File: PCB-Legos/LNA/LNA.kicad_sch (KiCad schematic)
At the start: 36 parts, among them J1 Conn_Coaxial, J2 Conn_Coaxial, J3 Conn_Coaxial, U1 LP2985XX-N, U2 LNA-TP3M9037, U3 QPQ1907, U4 LP2985XX-N, U5 LNA-TP3M9037, U6 QPQ1907

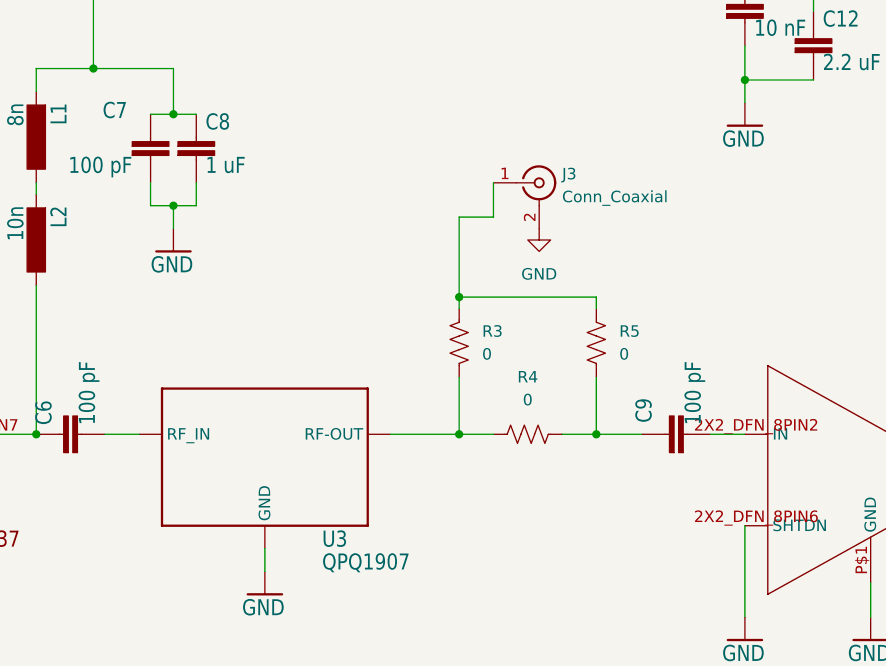
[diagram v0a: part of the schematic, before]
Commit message: LNA Test Board
LNA Test Board. Has ability to test each stage separately.
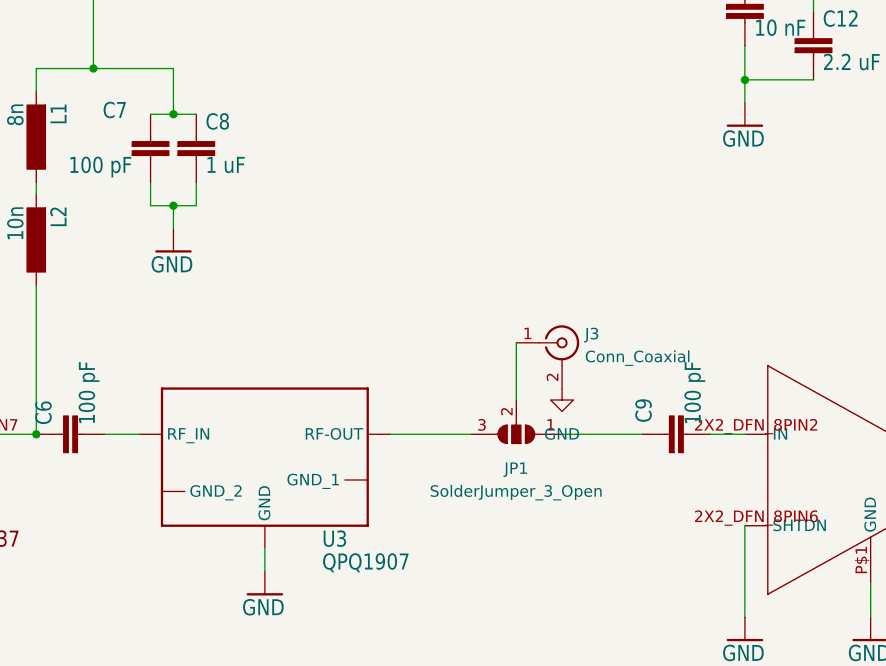
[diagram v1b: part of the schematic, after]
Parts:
- removed R3, R4, R5: 0, HGS_Reflector:.0603-B-NOSILK, symbol Device:R_US
- added JP1: SolderJumper_3_Open, Jumper:SolderJumper-3_P1.3mm_Open_Pad1.0x1.5mm_NumberLabels, symbol Jumper:SolderJumper_3_Open
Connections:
- net at U3.OUTPUT (RF-OUT): now also JP1.3 (B)
- net at C9.1: now also JP1.1 (A)
- net at J3.1 (In): now also JP1.2 (C)
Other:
- moved on the sheet: J3
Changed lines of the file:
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@@
   (junction (at 160.02 54.61) (diameter 0) (color 0 0 0 0)
   )
-  (junction (at 135.89 127) (diameter 0) (color 0 0 0 0)
-  )
   (junction (at 212.09 91.44) (diameter 0) (color 0 0 0 0)
   )
@@
   (junction (at 203.2 86.36) (diameter 0) (color 0 0 0 0)
   )
-  (junction (at 151.13 127) (diameter 0) (color 0 0 0 0)
-  )
-  (junction (at 135.89 111.76) (diameter 0) (color 0 0 0 0)
-  )
   (junction (at 167.64 87.63) (diameter 0) (color 0 0 0 0)
   )
@@
     (stroke (width 0) (type default) (color 0 0 0 0))
   )
-  (wire (pts (xy 128.27 127) (xy 135.89 127))
-    (stroke (width 0) (type default) (color 0 0 0 0))
-  )
-  (wire (pts (xy 135.89 111.76) (xy 151.13 111.76))
+  (wire (pts (xy 128.27 127) (xy 137.16 127))
     (stroke (width 0) (type default) (color 0 0 0 0))
   )
@@
     (stroke (width 0) (type default) (color 0 0 0 0))
   )
-  (wire (pts (xy 139.7 99.06) (xy 139.7 102.87))
-    (stroke (width 0) (type default) (color 0 0 0 0))
-  )
   (wire (pts (xy 224.79 144.78) (xy 224.79 147.32))
     (stroke (width 0) (type default) (color 0 0 0 0))
@@
     (stroke (width 0) (type default) (color 0 0 0 0))
   )
-  (wire (pts (xy 151.13 127) (xy 156.21 127))
-    (stroke (width 0) (type default) (color 0 0 0 0))
-  )
   (wire (pts (xy 67.31 140.97) (xy 67.31 138.43))
     (stroke (width 0) (type default) (color 0 0 0 0))
@@
     (stroke (width 0) (type default) (color 0 0 0 0))
   )
-  (wire (pts (xy 135.89 111.76) (xy 135.89 113.03))
-    (stroke (width 0) (type default) (color 0 0 0 0))
-  )
   (wire (pts (xy 199.39 132.08) (xy 196.85 132.08))
     (stroke (width 0) (type default) (color 0 0 0 0))
@@
     (stroke (width 0) (type default) (color 0 0 0 0))
   )
-  (wire (pts (xy 135.89 120.65) (xy 135.89 127))
-    (stroke (width 0) (type default) (color 0 0 0 0))
-  )
-  (wire (pts (xy 151.13 111.76) (xy 151.13 113.03))
-    (stroke (width 0) (type default) (color 0 0 0 0))
-  )
   (wire (pts (xy 59.69 90.17) (xy 59.69 87.63))
     (stroke (width 0) (type default) (color 0 0 0 0))
@@
     (stroke (width 0) (type default) (color 0 0 0 0))
   )
-  (wire (pts (xy 151.13 120.65) (xy 151.13 127))
-    (stroke (width 0) (type default) (color 0 0 0 0))
-  )
   (wire (pts (xy 67.31 44.45) (xy 67.31 40.64))
     (stroke (width 0) (type default) (color 0 0 0 0))
@@
     (stroke (width 0) (type default) (color 0 0 0 0))
   )
-  (wire (pts (xy 139.7 102.87) (xy 135.89 102.87))
-    (stroke (width 0) (type default) (color 0 0 0 0))
-  )
-  (wire (pts (xy 147.32 127) (xy 151.13 127))
+  (wire (pts (xy 147.32 127) (xy 156.21 127))
     (stroke (width 0) (type default) (color 0 0 0 0))
   )
@@
     (stroke (width 0) (type default) (color 0 0 0 0))
   )
+  (wire (pts (xy 142.24 116.84) (xy 142.24 123.19))
+    (stroke (width 0) (type default) (color 0 0 0 0))
+  )
   (wire (pts (xy 167.64 44.45) (xy 167.64 40.64))
     (stroke (width 0) (type default) (color 0 0 0 0))
@@
   )
   (wire (pts (xy 88.9 86.36) (xy 95.25 86.36))
-    (stroke (width 0) (type default) (color 0 0 0 0))
-  )
-  (wire (pts (xy 135.89 102.87) (xy 135.89 111.76))
-    (stroke (width 0) (type default) (color 0 0 0 0))
-  )
-  (wire (pts (xy 135.89 127) (xy 139.7 127))
     (stroke (width 0) (type default) (color 0 0 0 0))
   )
@@
     (pin "OUTPUT")
   )
-  (symbol (lib_id "power:GND") (at 144.78 104.14 0) (unit 1)
+  (symbol (lib_id "power:GND") (at 147.32 121.92 0) (unit 1)
     (in_bom yes) (on_board yes) (fields_autoplaced)
-    (property "Reference" "#PWR0102" (id 0) (at 144.78 110.49 0)
-      (effects (font (size 1.27 1.27)) hide)
-    )
-    (property "Value" "GND" (id 1) (at 144.78 109.22 0))
-    (property "Footprint" "" (id 2) (at 144.78 104.14 0)
-      (effects (font (size 1.27 1.27)) hide)
-    )
-    (property "Datasheet" "" (id 3) (at 144.78 104.14 0)
+    (property "Reference" "#PWR0102" (id 0) (at 147.32 128.27 0)
+      (effects (font (size 1.27 1.27)) hide)
+    )
+    (property "Value" "GND" (id 1) (at 147.32 127 0))
+    (property "Footprint" "" (id 2) (at 147.32 121.92 0)
+      (effects (font (size 1.27 1.27)) hide)
+    )
+    (property "Datasheet" "" (id 3) (at 147.32 121.92 0)
       (effects (font (size 1.27 1.27)) hide)
     )
@@
     (pin "2")
   )
-  (symbol (lib_id "Device:R_US") (at 143.51 127 90) (unit 1)
-    (in_bom yes) (on_board yes) (fields_autoplaced)
-    (property "Reference" "R4" (id 0) (at 143.51 120.65 90))
-    (property "Value" "0" (id 1) (at 143.51 123.19 90))
-    (property "Footprint" "HGS_Reflector:.0603-B-NOSILK" (id 2) (at 143.764 125.984 90)
-      (effects (font (size 1.27 1.27)) hide)
-    )
-    (property "Datasheet" "~" (id 3) (at 143.51 127 0)
-      (effects (font (size 1.27 1.27)) hide)
-    )
-    (pin "1")
-    (pin "2")
-  )
   (symbol (lib_id "HGS_Reflector-eagle-import:GND") (at 224.79 149.86 0) (unit 1)
     (in_bom yes) (on_board yes)
@@
     (pin "2")
   )
-  (symbol (lib_id "Connector:Conn_Coaxial") (at 144.78 99.06 0) (unit 1)
+  (symbol (lib_id "Connector:Conn_Coaxial") (at 147.32 116.84 0) (unit 1)
     (in_bom yes) (on_board yes) (fields_autoplaced)
-    (property "Reference" "J3" (id 0) (at 147.32 98.0831 0)
+    (property "Reference" "J3" (id 0) (at 149.86 115.8631 0)
       (effects (font (size 1.27 1.27)) (justify left))
     )
-    (property "Value" "Conn_Coaxial" (id 1) (at 147.32 100.6231 0)
+    (property "Value" "Conn_Coaxial" (id 1) (at 149.86 118.4031 0)
       (effects (font (size 1.27 1.27)) (justify left))
     )
-    (property "Footprint" "Connector_Coaxial:SMA_Molex_73251-1153_EdgeMount_Horizontal" (id 2) (at 144.78 99.06 0)
-      (effects (font (size 1.27 1.27)) hide)
-    )
-    (property "Datasheet" " ~" (id 3) (at 144.78 99.06 0)
+    (property "Footprint" "Connector_Coaxial:SMA_Molex_73251-1153_EdgeMount_Horizontal" (id 2) (at 147.32 116.84 0)
+      (effects (font (size 1.27 1.27)) hide)
+    )
+    (property "Datasheet" " ~" (id 3) (at 147.32 116.84 0)
       (effects (font (size 1.27 1.27)) hide)
     )
@@
     )
     (pin "1")
+  )
+  (symbol (lib_id "Jumper:SolderJumper_3_Open") (at 142.24 127 180) (unit 1)
+    (in_bom yes) (on_board yes) (fields_autoplaced)
+    (property "Reference" "JP1" (id 0) (at 142.24 130.81 0))
+    (property "Value" "SolderJumper_3_Open" (id 1) (at 142.24 133.35 0))
+    (property "Footprint" "Jumper:SolderJumper-3_P1.3mm_Open_Pad1.0x1.5mm_NumberLabels" (id 2) (at 142.24 127 0)
+      (effects (font (size 1.27 1.27)) hide)
+    )
+    (property "Datasheet" "~" (id 3) (at 142.24 127 0)
+      (effects (font (size 1.27 1.27)) hide)
+    )
+    (pin "1")
+    (pin "2")
+    (pin "3")
   )
   (symbol (lib_id "HGS_Reflector-eagle-import:GND") (at 181.61 149.86 0) (unit 1)
@@
     (pin "1")
   )
-  (symbol (lib_id "Device:R_US") (at 151.13 116.84 0) (unit 1)
-    (in_bom yes) (on_board yes) (fields_autoplaced)
-    (property "Reference" "R5" (id 0) (at 153.67 115.5699 0)
-      (effects (font (size 1.27 1.27)) (justify left))
-    )
-    (property "Value" "0" (id 1) (at 153.67 118.1099 0)
-      (effects (font (size 1.27 1.27)) (justify left))
-    )
-    (property "Footprint" "HGS_Reflector:.0603-B-NOSILK" (id 2) (at 152.146 117.094 90)
-      (effects (font (size 1.27 1.27)) hide)
-    )
-    (property "Datasheet" "~" (id 3) (at 151.13 116.84 0)
-      (effects (font (size 1.27 1.27)) hide)
-    )
-    (pin "1")
-    (pin "2")
-  )
   (symbol (lib_id "HGS_Reflector-eagle-import:VUSB") (at 243.84 44.45 180) (unit 1)
     (in_bom yes) (on_board yes)
@@
     (pin "1")
   )
-  (symbol (lib_id "Device:R_US") (at 135.89 116.84 0) (mirror y) (unit 1)
-    (in_bom yes) (on_board yes) (fields_autoplaced)
-    (property "Reference" "R3" (id 0) (at 138.43 115.5699 0)
-      (effects (font (size 1.27 1.27)) (justify right))
-    )
-    (property "Value" "0" (id 1) (at 138.43 118.1099 0)
-      (effects (font (size 1.27 1.27)) (justify right))
-    )
-    (property "Footprint" "HGS_Reflector:.0603-B-NOSILK" (id 2) (at 134.874 117.094 90)
-      (effects (font (size 1.27 1.27)) hide)
-    )
-    (property "Datasheet" "~" (id 3) (at 135.89 116.84 0)
-      (effects (font (size 1.27 1.27)) hide)
-    )
-    (pin "1")
-    (pin "2")
-  )
   (symbol (lib_id "HGS_Reflector-eagle-import:C-EU0402-C-NOSILK") (at 201.93 132.08 90) (unit 1)
     (in_bom yes) (on_board yes)
@@
     (pin "1")
   )
-  (symbol (lib_id "HGS_Reflector-eagle-import:QPQ1907") (at 114.3 129.54 0) (unit 1)
+  (symbol (lib_name "QPQ1907_1") (lib_id "HGS_Reflector-eagle-import:QPQ1907") (at 114.3 129.54 0) (unit 1)
     (in_bom yes) (on_board yes)
     (property "Reference" "U3" (id 0) (at 120.65 139.7 0)
@@
     (pin "INPUT")
     (pin "OUTPUT")
+    (pin "")
+    (pin "")
   )
   (sheet_instances
@@
       (reference "J3") (unit 1) (value "Conn_Coaxial") (footprint "Connector_Coaxial:SMA_Molex_73251-1153_EdgeMount_Horizontal")
     )
+    (path "/742f6656-c86d-41c0-937e-ef6ded3bd482"
+      (reference "JP1") (unit 1) (value "SolderJumper_3_Open") (footprint "Jumper:SolderJumper-3_P1.3mm_Open_Pad1.0x1.5mm_NumberLabels")
+    )
     (path "/29f4961c-cbd7-42a0-91e7-8ae77405e061"
       (reference "L1") (unit 1) (value "8n") (footprint "HGS_Reflector:L3216C")
@@
       (reference "R2") (unit 1) (value "0") (footprint "HGS_Reflector:.0603-B-NOSILK")
     )
-    (path "/ed452e4f-f8c6-4901-b871-cda6a9b3fcb3"
-      (reference "R3") (unit 1) (value "0") (footprint "HGS_Reflector:.0603-B-NOSILK")
-    )
-    (path "/226baf08-791d-4a76-8272-9455f91278e4"
-      (reference "R4") (unit 1) (value "0") (footprint "HGS_Reflector:.0603-B-NOSILK")
-    )
-    (path "/90cfdefd-60a4-4467-8596-d62808cfc899"
-      (reference "R5") (unit 1) (value "0") (footprint "HGS_Reflector:.0603-B-NOSILK")
-    )
     (path "/a0af1aa5-82ff-4825-8836-86496e7db65f"

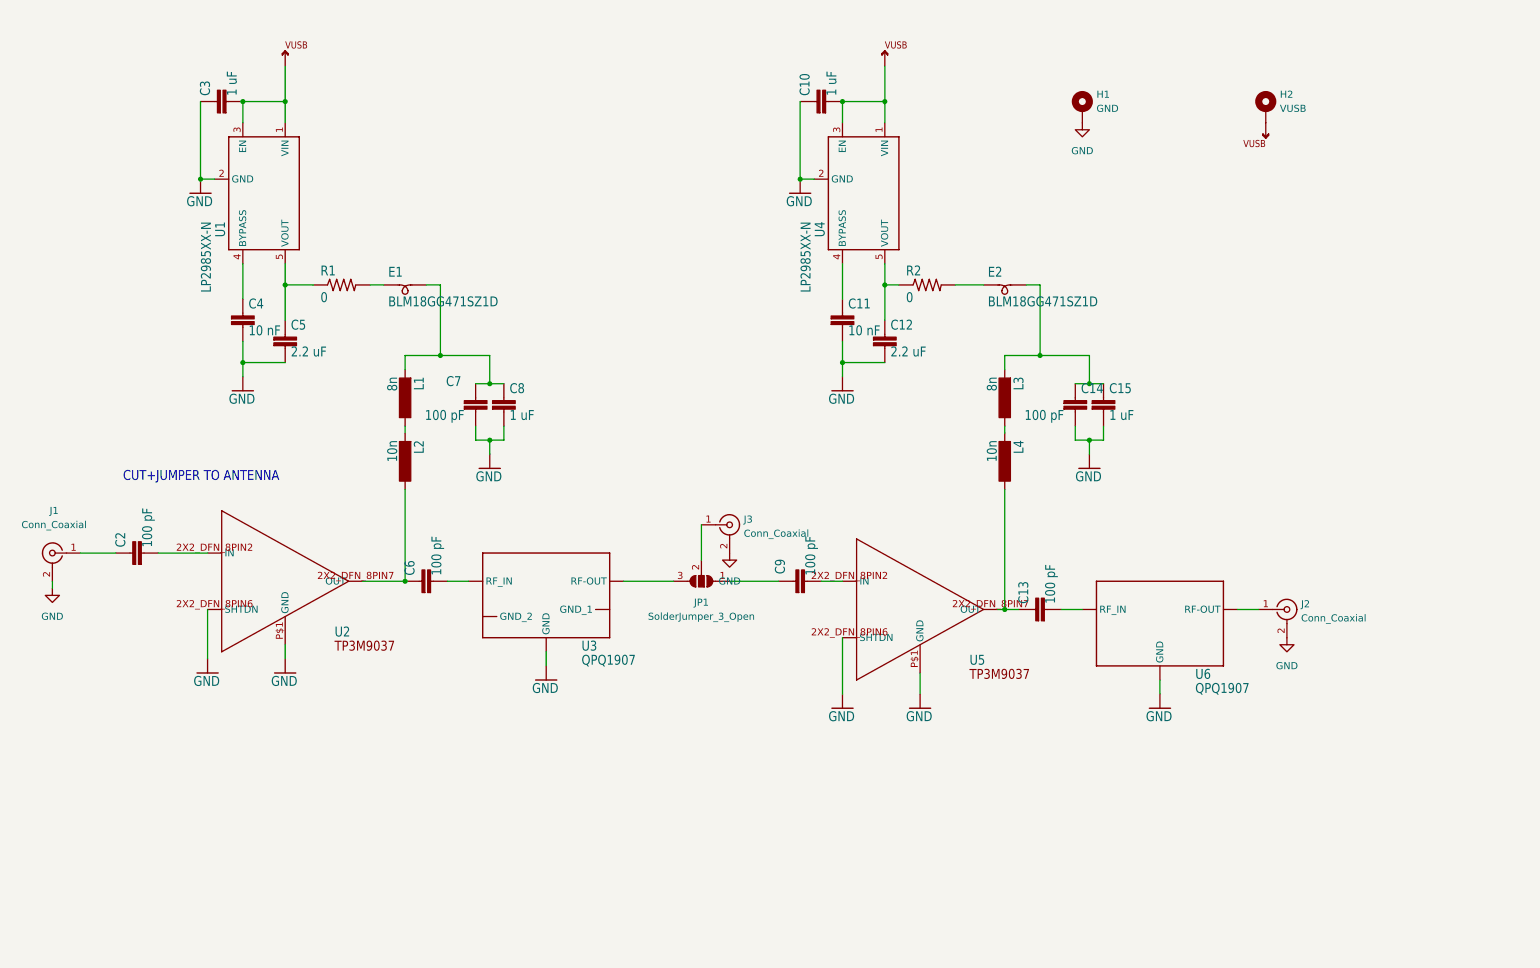
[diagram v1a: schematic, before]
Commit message: LNA Board
LNA Test board with ability to test each stage
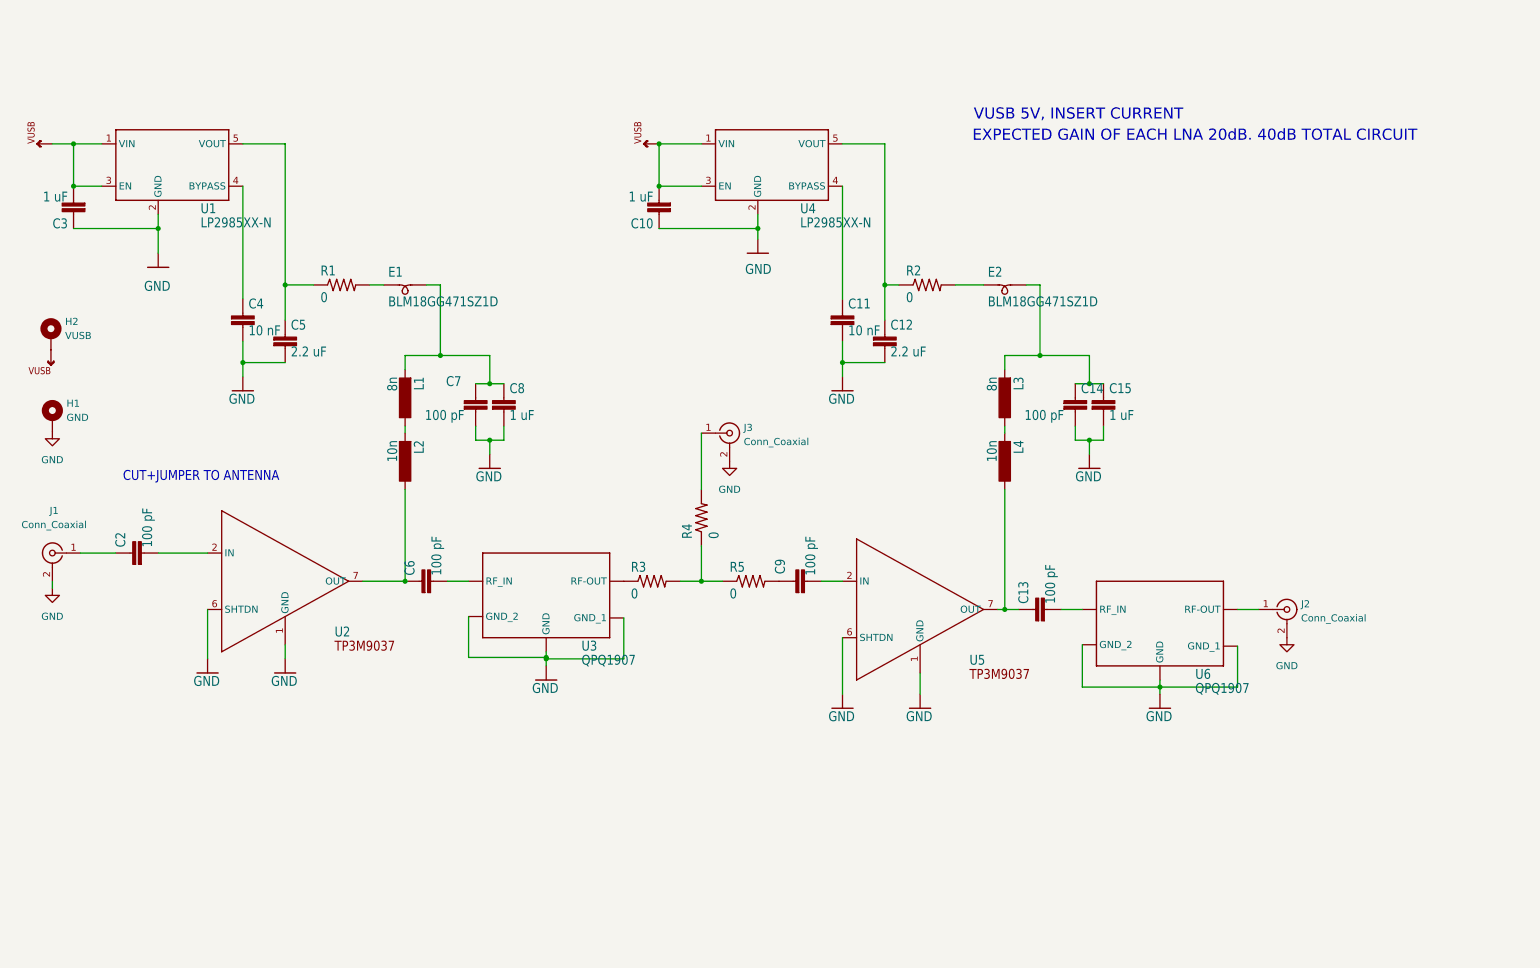
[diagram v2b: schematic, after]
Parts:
- removed JP1: SolderJumper_3_Open, Jumper:SolderJumper-3_P1.3mm_Open_Pad1.0x1.5mm_NumberLabels, symbol Jumper:SolderJumper_3_Open
- added R3, R4, R5: 0, HGS_Reflector:.0603-B-NOSILK, symbol HGS_Reflector-eagle-import:R-US_0603-B-NOSILK
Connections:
- net GND: now also U2.1 (GND), U2.6 (SHTDN), U3. (GND_2), U5.1 (GND), U5.6 (SHTDN), U6. (GND_2); no longer U2.2X2_DFN_8PIN6 (SHTDN), U2.P$1 (GND), U5.2X2_DFN_8PIN6 (SHTDN), U5.P$1 (GND)
- net at C6.1, L2.1: now also U2.7 (OUT); no longer U2.2X2_DFN_8PIN7 (OUT)
- net at J3.1 (In): now also R4.2
- net at C2.2: now also U2.2 (IN); no longer U2.2X2_DFN_8PIN2 (IN)
- net at C9.1: now also R5.2
- net at U3.OUTPUT (RF-OUT): now also R3.1
- net at C13.1, L4.1: now also U5.7 (OUT); no longer U5.2X2_DFN_8PIN7 (OUT)
- net at C9.2: now also U5.2 (IN); no longer U5.2X2_DFN_8PIN2 (IN)
- new net: R3.2, R4.1, R5.1
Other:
- note added: "EXPECTED GAIN OF EACH LNA 20dB. 40dB TOTAL CIRCUIT"
- note added: "VUSB 5V, INSERT CURRENT"
- moved on the sheet: C10, C3, H1, H2, J3, U1, U2, U4, U5
